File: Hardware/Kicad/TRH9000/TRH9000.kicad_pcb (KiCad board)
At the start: 2 copper layers, 99.1 x 63.5 mm, 74 parts, among them J1 RGB, J2 Console5_SCART, Q1 BC817, U1 V9990, U2 KM428C256, U3 KM428C256, U4 74VHC138, U5 T.I_SN74AHCT32D, U6 LMH1980, U7 T.I_SN74AHCT32D, X1 Crystek_CE3291, Y1 21.47727Mhz

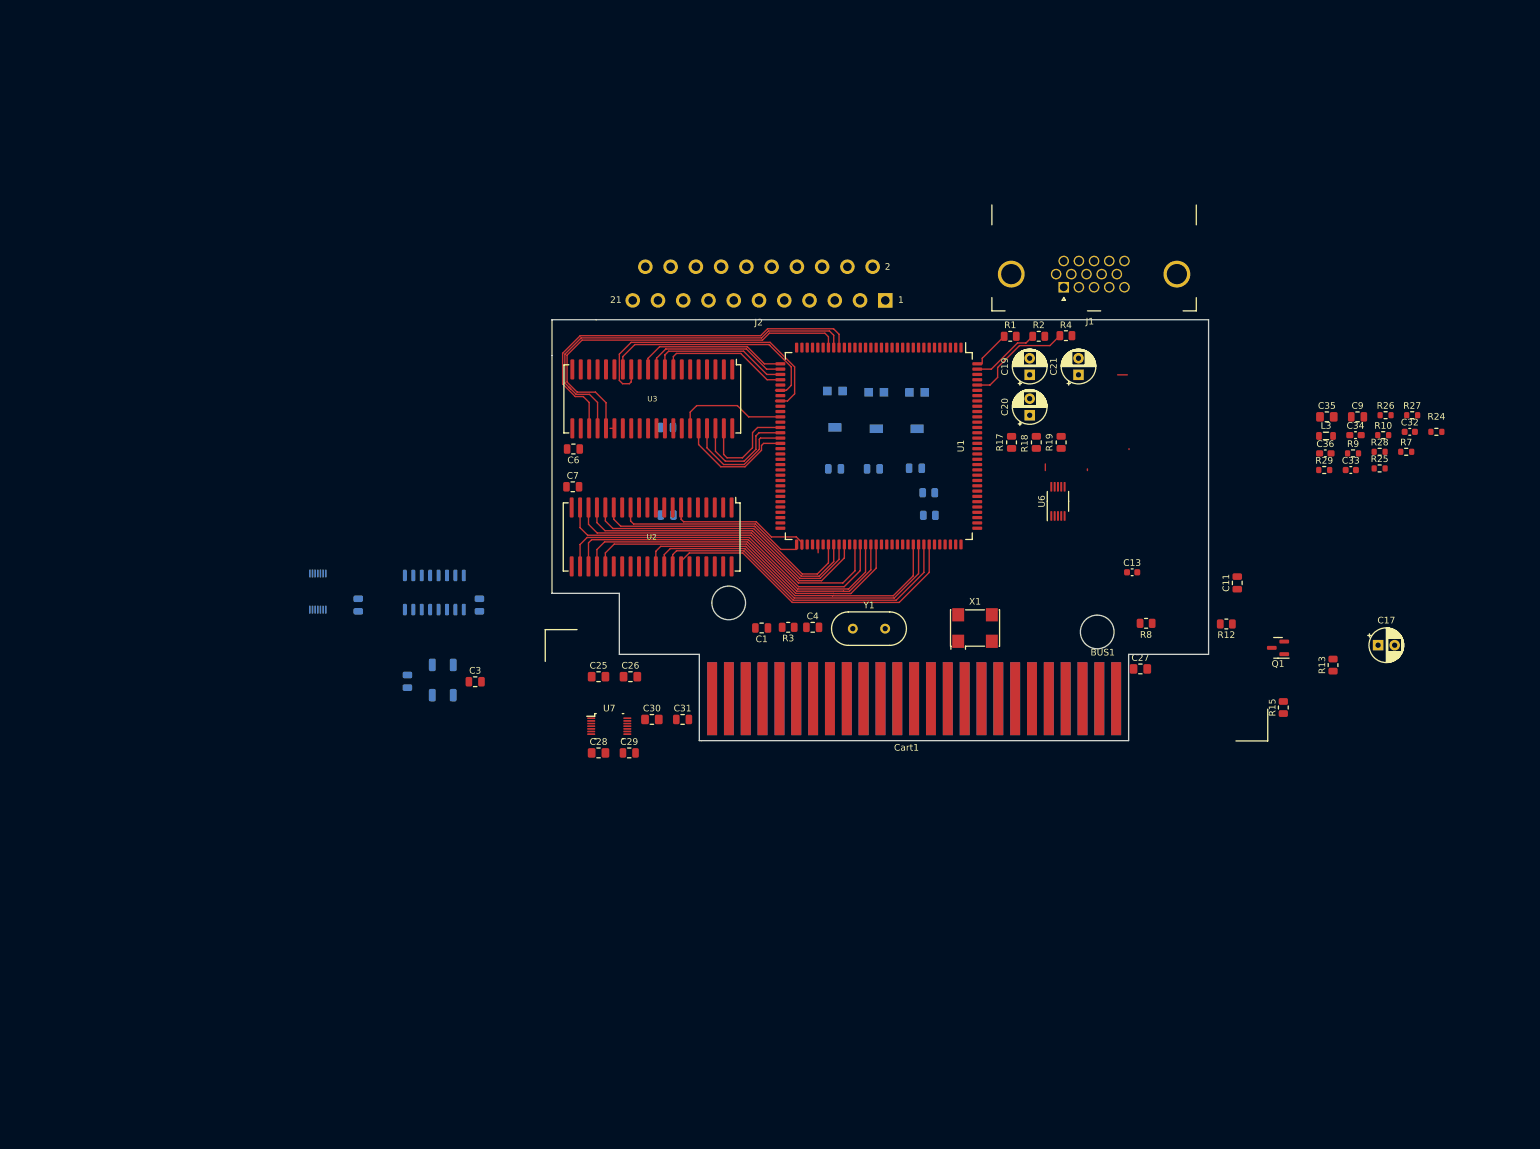
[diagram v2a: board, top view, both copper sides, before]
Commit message: Multiple updates. Routing. Almost finished routing for the VDP. Moved back the footprint for the 14mhz oscillator to THT as it is easier to find outside US/Europe and I have a bunch laying around here. Organized all components into the PCB. Removed the holed in the cartridge so I can better measure them in the standard MSX cartridge. Changed the RGB connector footprint to a shorter version so we can fit it in the standard size cartridge. Fixed multiple footprints to 0805 as we will be standardizing in that size.
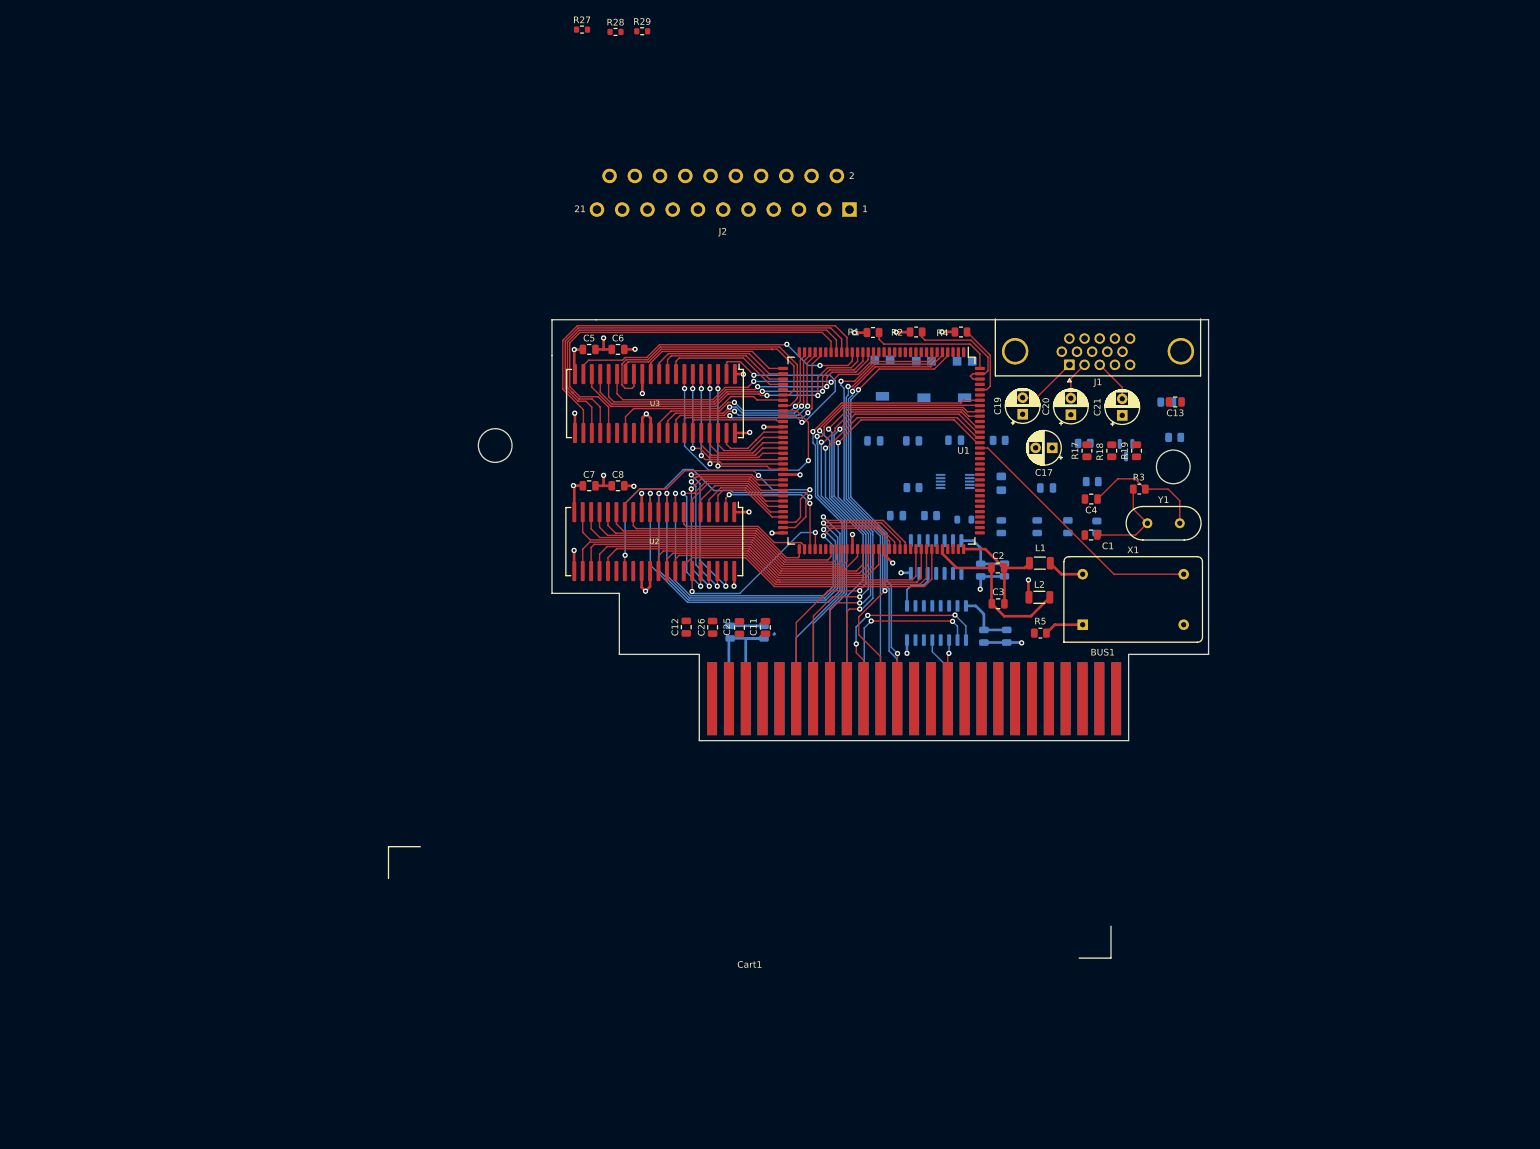
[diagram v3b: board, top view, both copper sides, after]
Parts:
- removed C9: 47pF, Capacitor_SMD:C_0805_2012Metric
- removed R7: R_ERJ-3GEYJ105V, Resistor_SMD:R_0603_1608Metric
- removed R8: 2K2, Resistor_SMD:R_0805_2012Metric
- removed the U7 at (106.9, 124.8)
- C10, C11, C7: value C_CC0805JPX7R9BB104 -> 0.1uF
- C12, C5: value C_CC0805JPX7R9BB104 -> 0.1uF; moved to F.Cu
- C13: value C_GRM188D71A106KA73D -> 10µF; footprint Capacitor_SMD:C_0603_1608Metric -> Capacitor_SMD:C_0805_2012Metric
- C2, C8, L1, L2, R5: moved to F.Cu
- C25, C26: value C_CL21B105KBFNNNF -> 1 µF; footprint Capacitor_SMD:C_0805_2012Metric_Pad1.18x1.45mm_HandSolder -> Capacitor_SMD:C_0805_2012Metric
- C27, C28, C30: value C_CL21B105KBFNNNF -> 1 µF; footprint Capacitor_SMD:C_0805_2012Metric_Pad1.18x1.45mm_HandSolder -> Capacitor_SMD:C_0805_2012Metric; moved to B.Cu
- C29, C31: value C_CC0805JPX7R9BB104 -> 0.1uF; moved to B.Cu
- C3: value C_GRM21BR61A476ME15K -> 47uF
- C32, C33: footprint Capacitor_SMD:C_0603_1608Metric -> Capacitor_SMD:C_0805_2012Metric; moved to B.Cu
- C34, C36: value C_CL10B104KB8NNNL -> 0.1µF; footprint Capacitor_SMD:C_0603_1608Metric_Pad1.08x0.95mm_HandSolder -> Capacitor_SMD:C_0805_2012Metric; moved to B.Cu
- C35: value C_GRM21BR71A106KA73K -> 10uF; moved to B.Cu
- J1: footprint LRJ:DSUB-Amphenol_L77HDE15SD1CH4RHNVGA -> Connector_Dsub:DSUB-15-HD_Female_Horizontal_P2.29x1.98mm_EdgePinOffset3.03mm_Housed_MountingHolesOffset4.94mm
- L3: value L_MLZ2012M4R7HT000 -> 4.7µH; moved to B.Cu
- Q1, R12, R13, R15, U6: moved to B.Cu
- R10, R25, R26, R9: footprint Resistor_SMD:R_0603_1608Metric -> Resistor_SMD:R_0805_2012Metric; moved to B.Cu
- R24: value R_RC0603FR-0710KL -> 10k; footprint LRJ:R_0603_1608Metric_roundcourt -> Capacitor_SMD:C_0805_2012Metric; moved to B.Cu
- U4: value 74VHC138 -> 74HC138
- U7: renamed from U5; value T.I_SN74AHCT32D -> 74HC32; footprint trh9000:Texas_R-PDSO-G14_3.6x4.4mm -> Package_SO:SO-14_3.9x8.65mm_P1.27mm
- X1: value Crystek_CE3291 -> 14.31818MHz; footprint Oscillator:Oscillator_SMD_Abracon_ASV-4Pin_7.0x5.1mm -> Oscillator:Oscillator_DIP-14
- moved R27 138.1 mm to (102.8, 19.7)
- moved R28 131.5 mm to (107.8, 20.1)
- moved R29 122.3 mm to (111.9, 20.0)
- moved U7 93.4 mm to (156.2, 99.3)
- moved L1 91.4 mm to (171.9, 100.2)
- moved L2 91.2 mm to (171.8, 105.4), turned to 0 degrees
- moved C2 90.7 mm to (165.5, 101.0), turned to 180 degrees
- moved R24 82.4 mm to (150.2, 93.0)
- moved C3 79.8 mm to (165.6, 106.3), turned to 180 degrees
- moved U4 75.9 mm to (156.3, 109.2)
- moved R26 72.1 mm to (152.7, 88.8)
- moved C11 71.5 mm to (130.5, 109.9), turned to -90 degrees
- moved R25 68.1 mm to (155.4, 93.0)
- moved C28 64.1 mm to (166.9, 111.2), turned to -90 degrees
- moved C30 57.8 mm to (166.5, 101.2), turned to -90 degrees
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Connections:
- U7 pad 14: (no net) -> +5V
- U7 pad 7: (no net) -> GND
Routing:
- net +5V: track 0.00 -> 84.2 mm, vias 0 -> 11
- net /D6: track 0.00 -> 76.4 mm, vias 0 -> 2
- net /D4: track 0.00 -> 73.6 mm, vias 0 -> 2
- net /VDP/V1D3: track 0.00 -> 72.4 mm, vias 0 -> 2
- net /D7: track 0.00 -> 72.1 mm, vias 0 -> 1
- net /D2: track 0.00 -> 71.4 mm, vias 0 -> 2
- net /D5: track 0.00 -> 70.6 mm, vias 0 -> 1
- net /VDP/V1D2: track 0.00 -> 68.6 mm, vias 0 -> 2
- net /A2: track 0.00 -> 68.5 mm, vias 0 -> 2
- net /D3: track 0.00 -> 68.3 mm, vias 0 -> 1
- net /D0: track 0.00 -> 67.7 mm, vias 0 -> 2
- net /D1: track 0.00 -> 67.6 mm, vias 0 -> 1
- net GND: track 0.00 -> 67.1 mm, vias 0 -> 18
- net /A3: track 0.00 -> 66.3 mm, vias 0 -> 1
- net /A1: track 0.00 -> 66.3 mm, vias 0 -> 1
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- added copper zone on In2.Cu, net +5V
- added copper zone on In1.Cu, net GND
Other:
- board size 99.1 x 63.5 mm -> 110.2 x 63.5 mm
- copper layers 2 -> 4

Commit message: Routing, readme, etc
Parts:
- removed C11, C12: 0.1uF, Capacitor_SMD:C_0805_2012Metric
- removed C25, C26: 1 µF, Capacitor_SMD:C_0805_2012Metric
- removed J2: Console5_SCART, LRJ:SCART-21_Female_Horizontal_P1.905x2.54mm_EdgePinOffset10.7mm
- removed R27, R28: 100, Resistor_SMD:R_0603_1608Metric
- removed R29: 1k, Resistor_SMD:R_0603_1608Metric
- added G***: LOGO, trh9000:TRH, B.Cu at (113.4, 72.3)
- added REF**: OSHW-Logo_11.4x12mm_SilkScreen, Symbol:OSHW-Logo_11.4x12mm_SilkScreen, B.Cu at (126.3, 72.4)
- R6: moved to F.Cu
- X1: footprint Oscillator:Oscillator_DIP-14 -> Oscillator:Oscillator_DIP-8
- moved Cart1 61.7 mm to (71.5, 176.2)
- moved R6 26.7 mm to (169.1, 91.1), turned to 0 degrees
- moved C36 24.8 mm to (159.2, 70.9)
- moved C13 21.9 mm to (171.5, 82.7), turned to 0 degrees
- moved R9 21.6 mm to (166.0, 78.7), turned to 90 degrees
- moved C33 21.2 mm to (166.0, 74.2)
- moved R26 19.4 mm to (144.6, 71.2)
- moved U6 18.7 mm to (151.8, 70.7)
- moved L3 18.2 mm to (157.0, 75.8)
- moved R24 17.6 mm to (146.4, 75.8)
- moved R25 17.6 mm to (151.6, 75.8), turned to 180 degrees
- moved C35 17.5 mm to (163.0, 70.9), turned to -90 degrees
- moved R12 16.7 mm to (182.3, 83.5)
- moved R13 16.2 mm to (176.2, 83.5)
- moved C32 15.8 mm to (166.0, 82.6), turned to 90 degrees
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- renumbered RV1 to RV1-R, RV2 to RV2-G, RV3 to RV3-B
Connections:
- X1 pad 8: /VDP/MCKIN -> +5V
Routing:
- net GNDA: track 25.1 -> 116.9 mm, vias 0 -> 2
- net GND: track 67.1 -> 147.6 mm, vias 18 -> 37
- net /~{WAIT}: track 19.3 -> 84.5 mm, vias 0 -> 3
- net /~{INT}: track 18.7 -> 81.0 mm, vias 0 -> 4
- net +5VA: track 16.8 -> 78.6 mm, vias 0 -> 3
- net /~{RESET}: track 0.00 -> 47.0 mm, vias 0 -> 1
- net /VDP/~{VDPR}: track 0.00 -> 45.7 mm, vias 0 -> 3
- net /VIDEO/VSYNC: track 0.00 -> 42.9 mm
- net /VDP/~{VDPW}: track 0.00 -> 42.5 mm, vias 0 -> 3
- net /SYS_CLK: track 0.00 -> 41.4 mm, vias 0 -> 1
- net /VIDEO/HSYNC: track 0.00 -> 39.6 mm
- net Net-(C17-Pad2): track 0.00 -> 36.8 mm, vias 0 -> 1
- net /VIDEO/RO: track 0.00 -> 35.4 mm, vias 0 -> 1
- net /VIDEO/CSYNCO: track 0.00 -> 34.7 mm, vias 0 -> 2
- net /VIDEO/GO: track 0.00 -> 32.9 mm, vias 0 -> 1
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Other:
- board size 110.2 x 63.5 mm -> 99.1 x 63.5 mm
- board text added: "The Yamaha V9990 open-source video card for the MSX Rev 1"
- board text removed: "The Yamaha V9990 open-source video card for the MSX"

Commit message: MSX logo
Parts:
- added G***: LOGO, LOGO, B.Cu at (106.3, 72.0)
- moved G*** 3.25 mm to (116.7, 72.2)
- moved REF** 1.55 mm to (127.8, 72.3)
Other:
- board text added: "Designed by the MSX community for the MSX community."

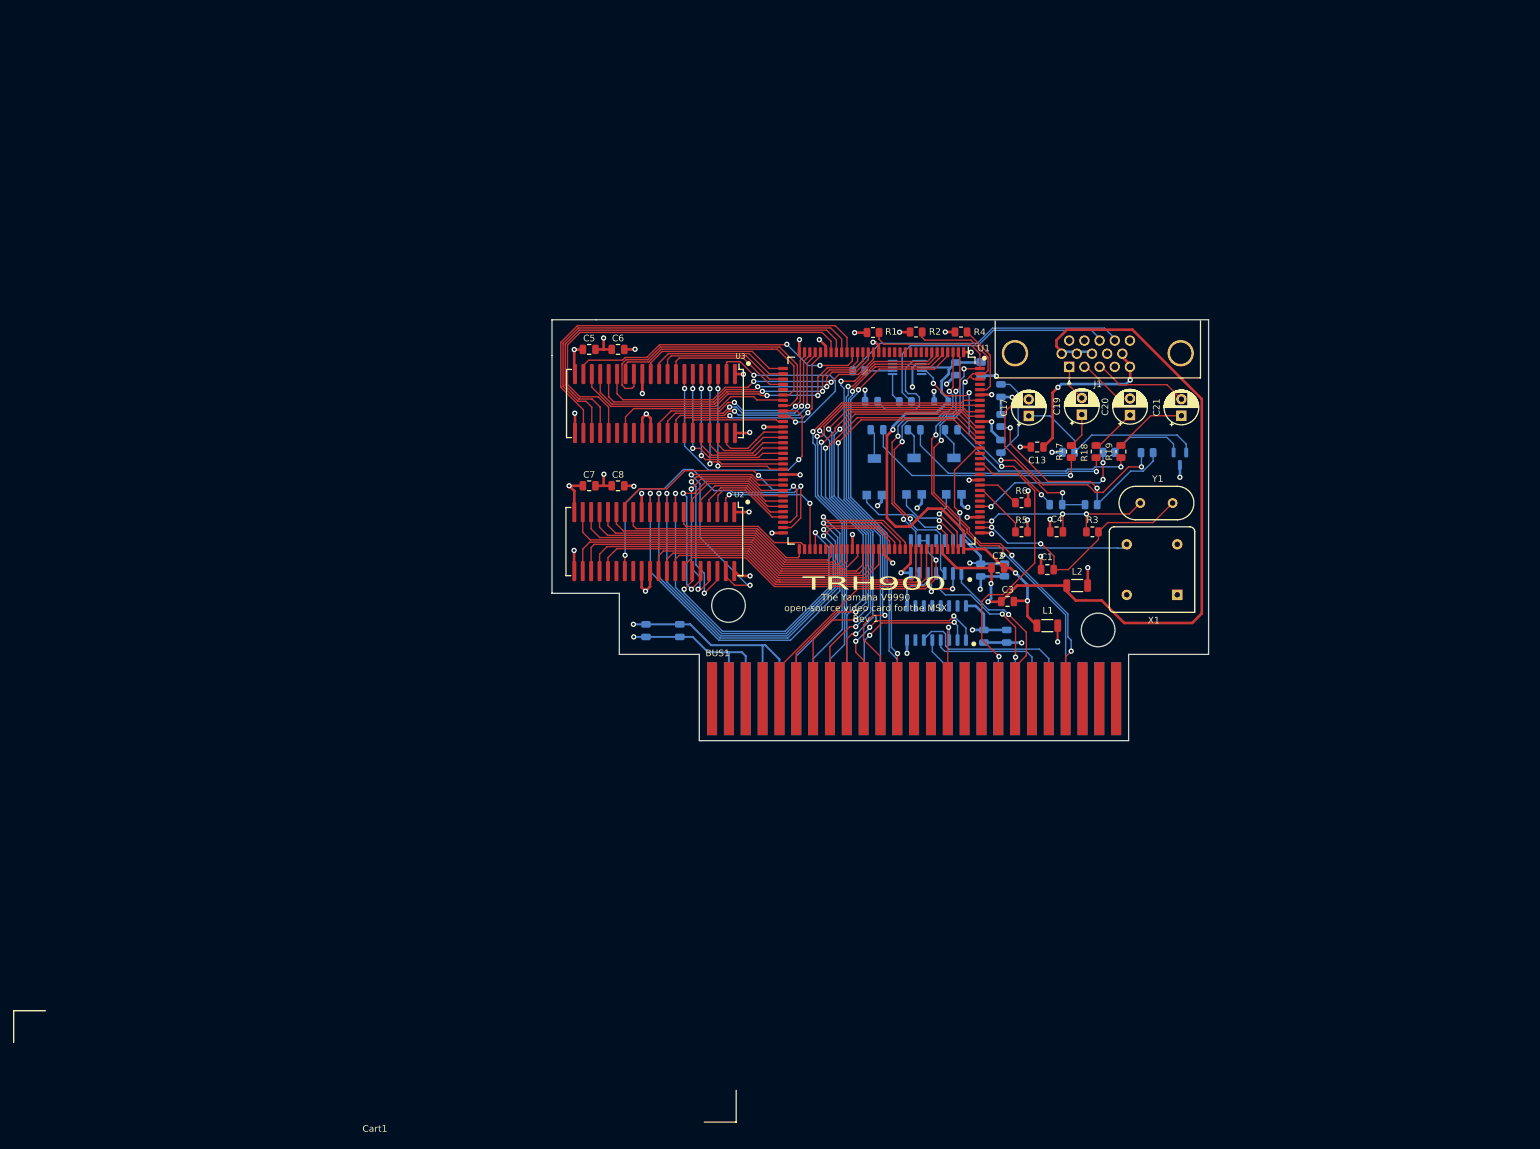
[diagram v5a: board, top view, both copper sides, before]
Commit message: Small correction on the front silkscreen
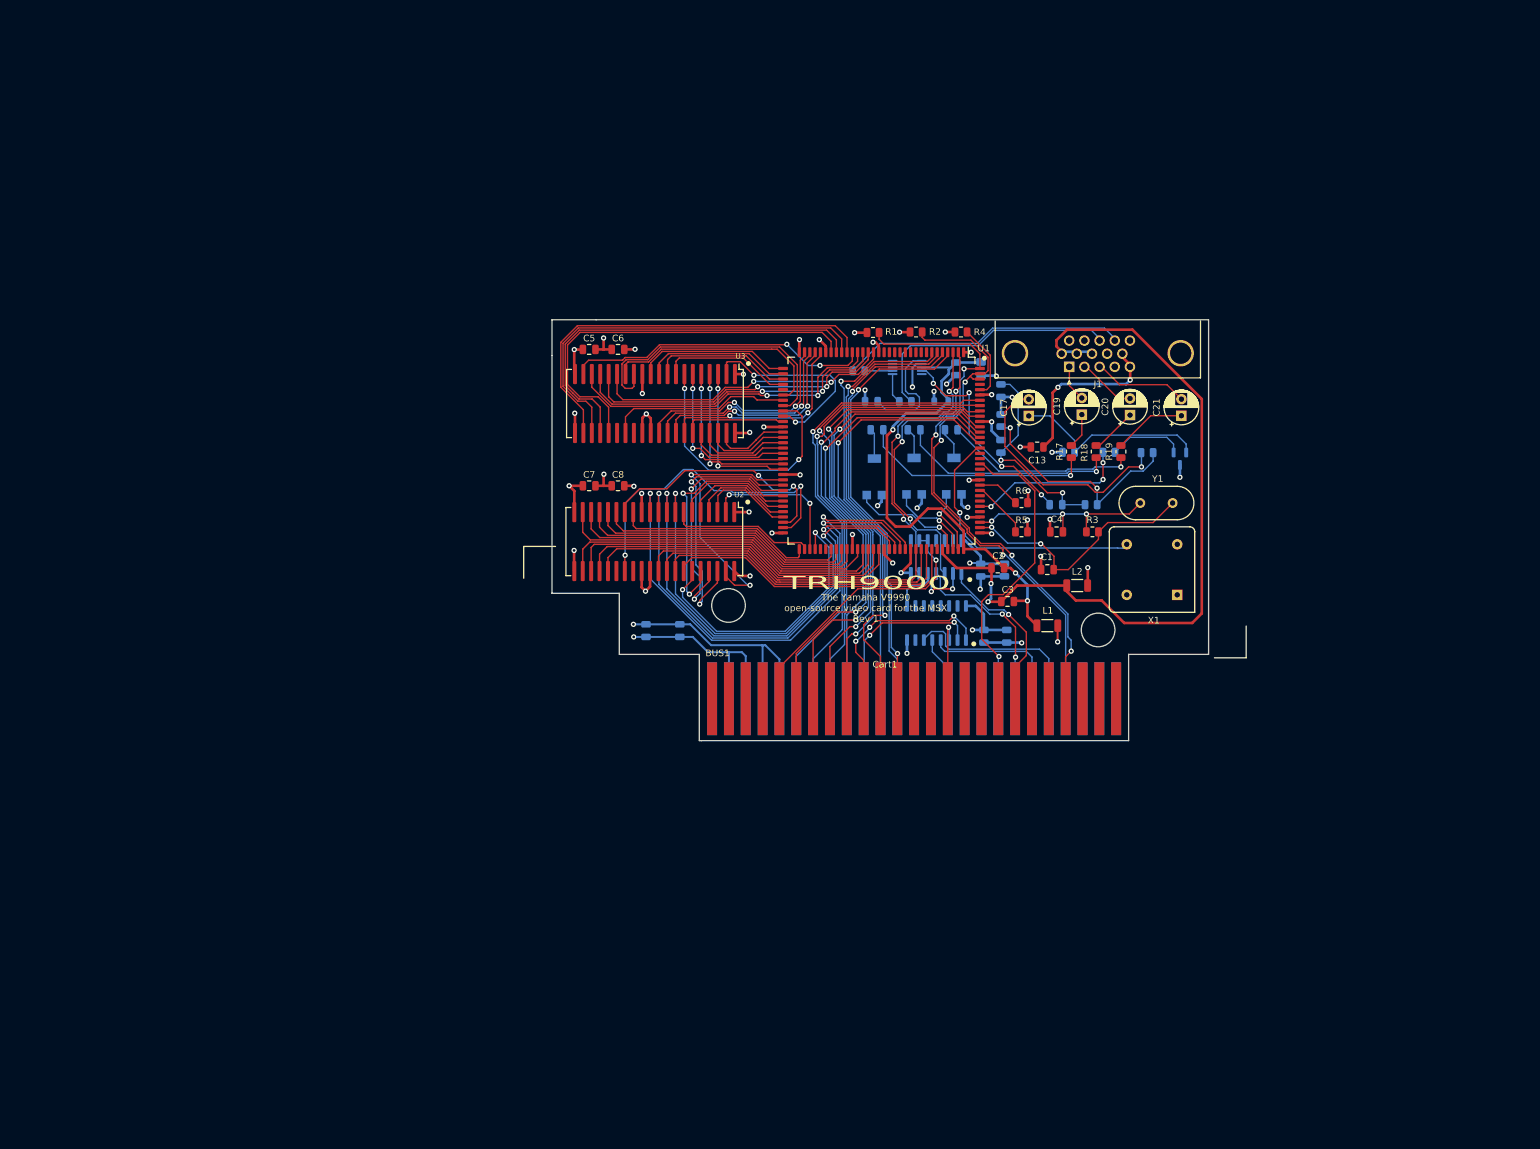
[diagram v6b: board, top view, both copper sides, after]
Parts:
- moved Cart1 104.1 mm to (148.5, 106.1)
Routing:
- net /VDP/V1S6: track 36.4 -> 40.0 mm
- net /VDP/V1S5: track 34.7 -> 37.9 mm
- net /VDP/V1S4: track 35.0 -> 36.5 mm
- net /VDP/~{V1_SOE}: track 42.5 -> 43.2 mm
- net /VDP/V1D3: track 77.7 -> 78.4 mm
- net /VDP/V1D2: track 74.0 -> 74.6 mm
- net /VDP/V1D1: track 70.5 -> 71.1 mm
- net /VDP/V1D0: track 67.3 -> 67.9 mm
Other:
- board text added: "TRH9000"
- board text removed: "TRH900"
